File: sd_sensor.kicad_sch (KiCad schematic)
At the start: 0 parts

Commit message: Ajout des composants + connexion page "SD + Sensor"
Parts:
- added C401, C402: 100n, symbol Device:C
- added J401: SHOU HAN TF-CARD H1.8, tuto-kicad-temp-logger:SHOUHAN_TF_CARD_H1.8, symbol tuto-kicad-temp-logger:SHOUHAN_TF_CARD_H1.8
- added R401: 1k, symbol Device:R
- added R402, R403: 10k, symbol Device:R
- added TP401, TP402, TP403, TP404, TP405: TestPoint, symbol Connector:TestPoint
- added U401: TMP102xxDRL, Package_TO_SOT_SMD:SOT-563, symbol Sensor_Temperature:TMP102xxDRL
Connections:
- new net: C402.1, R401.2, U401.5 (V+)
- new net +3V3: C401.1, J401.4 (VDD), R401.1, R402.1, R403.1
- new net GND: C401.2, C402.2, J401.6 (VSS), J401.SH (SHIELD), U401.2 (GND), U401.4 (ADD0)
- new net I2C.SCL: U401.1 (SCL)
- new net I2C.SDA: U401.6 (SDA)
- new net SD.CD: J401.9 (CD), R403.2, TP405.1
- new net SD.CS: J401.2 (CD/DAT3), R402.2, TP401.1
- new net SD.MISO: J401.7 (DAT0), TP404.1
- new net SD.MOSI: J401.3 (CMD), TP402.1
- new net SD.SCK: J401.5 (CLK), TP403.1
- no-connect marks 0 -> 3

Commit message: Vérification des règles électriques
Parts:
- C401, C402: footprint (none) -> Capacitor_SMD:C_0402_1005Metric
- R401, R402, R403: footprint (none) -> Resistor_SMD:R_0402_1005Metric
- TP401, TP402, TP403, TP404, TP405: footprint (none) -> TestPoint:TestPoint_Pad_D2.0mm
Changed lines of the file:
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@@
 			)
 		)
-		(property "Footprint" ""
+		(property "Footprint" "TestPoint:TestPoint_Pad_D2.0mm"
 			(at 69.85 160.02 0)
 			(effects
@@
 			)
 		)
-		(property "Footprint" ""
+		(property "Footprint" "Capacitor_SMD:C_0402_1005Metric"
 			(at 49.2252 60.96 0)
 			(effects
@@
 			)
 		)
-		(property "Footprint" ""
+		(property "Footprint" "Resistor_SMD:R_0402_1005Metric"
 			(at 52.832 137.16 90)
 			(effects
@@
 			)
 		)
-		(property "Footprint" ""
+		(property "Footprint" "TestPoint:TestPoint_Pad_D2.0mm"
 			(at 69.85 157.48 0)
 			(effects
@@
 			)
 		)
-		(property "Footprint" ""
+		(property "Footprint" "TestPoint:TestPoint_Pad_D2.0mm"
 			(at 69.85 152.4 0)
 			(effects
@@
 			)
 		)
-		(property "Footprint" ""
+		(property "Footprint" "TestPoint:TestPoint_Pad_D2.0mm"
 			(at 69.85 154.94 0)
 			(effects
@@
 			)
 		)
-		(property "Footprint" ""
+		(property "Footprint" "Resistor_SMD:R_0402_1005Metric"
 			(at 202.692 59.69 90)
 			(effects
@@
 			)
 		)
-		(property "Footprint" ""
+		(property "Footprint" "TestPoint:TestPoint_Pad_D2.0mm"
 			(at 69.85 149.86 0)
 			(effects
@@
 			)
 		)
-		(property "Footprint" ""
+		(property "Footprint" "Capacitor_SMD:C_0402_1005Metric"
 			(at 205.4352 73.66 0)
 			(effects
@@
 			)
 		)
-		(property "Footprint" ""
+		(property "Footprint" "Resistor_SMD:R_0402_1005Metric"
 			(at 61.722 137.16 90)
 			(effects
@@
 		)
 		(property "Value" "SHOU HAN TF-CARD H1.8"
-			(at 84.836 104.394 0)
-			(effects
-				(font
+			(at 84.836 103.886 0)
+			(effects
+				(font

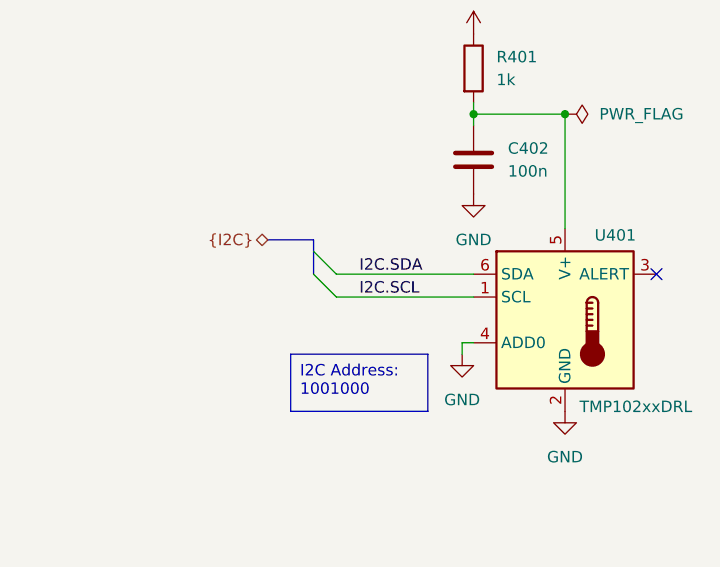
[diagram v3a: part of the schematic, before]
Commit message: Placement des composants
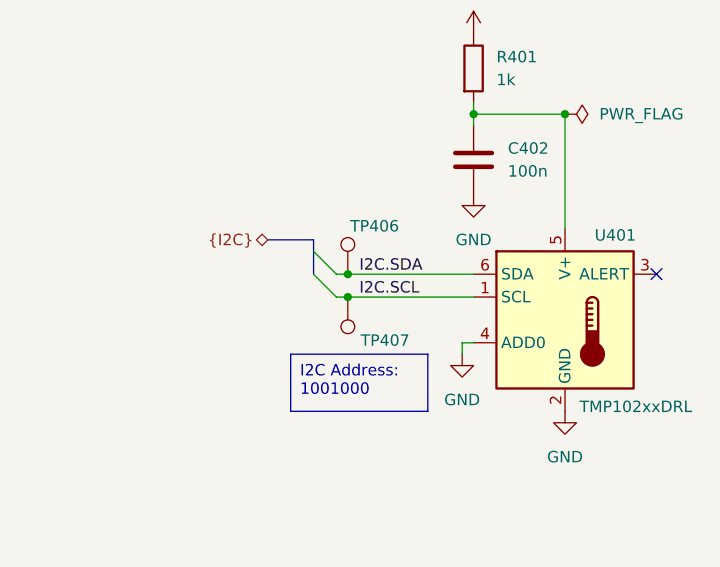
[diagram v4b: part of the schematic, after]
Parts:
- added TP406, TP407: TestPoint, TestPoint:TestPoint_Pad_D2.0mm, symbol Connector:TestPoint
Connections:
- net I2C.SCL: now also TP407.1
- net I2C.SDA: now also TP406.1
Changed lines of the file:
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@@
+	)
+	(junction
+		(at 190.5 85.09)
+		(diameter 0)
+		(color 0 0 0 0)
 	)
 	(junction
@@
 		(color 0 0 0 0)
 	)
+	(junction
+		(at 190.5 82.55)
+		(diameter 0)
+		(color 0 0 0 0)
+	)
 	(no_connect
 		(at 224.79 82.55)
@@
 	(wire
 		(pts
-			(xy 189.23 82.55) (xy 204.47 82.55)
+			(xy 189.23 82.55) (xy 190.5 82.55)
 		)
 		(stroke
@@
 	(wire
 		(pts
-			(xy 189.23 85.09) (xy 204.47 85.09)
+			(xy 189.23 85.09) (xy 190.5 85.09)
 		)
 		(stroke
@@
 	(wire
 		(pts
+			(xy 190.5 82.55) (xy 204.47 82.55)
+		)
+		(stroke
+			(width 0)
+			(type default)
+		)
+	)
+	(wire
+		(pts
 			(xy 74.93 105.41) (xy 77.47 105.41)
 		)
@@
 		(pts
 			(xy 214.63 64.77) (xy 214.63 77.47)
+		)
+		(stroke
+			(width 0)
+			(type default)
+		)
+	)
+	(wire
+		(pts
+			(xy 190.5 85.09) (xy 204.47 85.09)
 		)
 		(stroke
@@
 	)
 	(symbol
+		(lib_id "Connector:TestPoint")
+		(at 190.5 85.09 180)
+		(unit 1)
+		(exclude_from_sim no)
+		(in_bom yes)
+		(on_board yes)
+		(dnp no)
+		(property "Reference" "TP407"
+			(at 197.358 89.916 0)
+			(effects
+				(font
+					(size 1.27 1.27)
+				)
+				(justify left)
+			)
+		)
+		(property "Value" "TestPoint"
+			(at 187.96 87.1221 0)
+			(effects
+				(font
+					(size 1.27 1.27)
+				)
+				(justify left)
+				(hide yes)
+			)
+		)
+		(property "Footprint" "TestPoint:TestPoint_Pad_D2.0mm"
+			(at 185.42 85.09 0)
+			(effects
+				(font
+					(size 1.27 1.27)
+				)
+				(hide yes)
+			)
+		)
+		(property "Datasheet" "~"
+			(at 185.42 85.09 0)
+			(effects
+				(font
+					(size 1.27 1.27)
+				)
+				(hide yes)
+			)
+		)
+		(property "Description" "test point"
+			(at 190.5 85.09 0)
+			(effects
+				(font
+					(size 1.27 1.27)
+				)
+				(hide yes)
+			)
+		)
+		(pin "1"
+		)
+		(instances
+			(project "tuto-kicad-temp-logger"
+				(path "/46f6f3f4-3d30-4d83-91be-742ee6806614/dab7cd41-1874-4413-9892-b5d7fb28604f"
+					(reference "TP407")
+					(unit 1)
+				)
+			)
+		)
+	)
+	(symbol
 		(lib_id "power:+3V3")
 		(at 54.61 133.35 0)
@@
 					(unit 1)
 				)
+			)
+		)
+	)
+	(symbol
+		(lib_id "Connector:TestPoint")
+		(at 190.5 82.55 0)
+		(unit 1)
+		(exclude_from_sim no)
+		(in_bom yes)
+		(on_board yes)
+		(dnp no)
+		(property "Reference" "TP406"
+			(at 190.754 77.216 0)
+			(effects
+				(font
+					(size 1.27 1.27)
+				)
+				(justify left)
+			)
+		)
+		(property "Value" "TestPoint"
+			(at 193.04 80.5179 0)
+			(effects
+				(font
+					(size 1.27 1.27)
+				)
+				(justify left)
+				(hide yes)
+			)
+		)
+		(property "Footprint" "TestPoint:TestPoint_Pad_D2.0mm"
+			(at 195.58 82.55 0)
+			(effects
+				(font
+					(size 1.27 1.27)
+				)
+				(hide yes)
+			)
+		)
+		(property "Datasheet" "~"
+			(at 195.58 82.55 0)
+			(effects
+				(font
+					(size 1.27 1.27)
+				)
+				(hide yes)
+			)
+		)
+		(property "Description" "test point"
+			(at 190.5 82.55 0)
+			(effects
+				(font
+					(size 1.27 1.27)
+				)
+				(hide yes)
+			)
+		)
+		(pin "1"
+		)
+		(instances
+			(project "tuto-kicad-temp-logger"
+				(path "/46f6f3f4-3d30-4d83-91be-742ee6806614/dab7cd41-1874-4413-9892-b5d7fb28604f"
+					(reference "TP406")
+					(unit 1)
+				)
